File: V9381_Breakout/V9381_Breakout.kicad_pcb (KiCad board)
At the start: 2 copper layers, 38.1 x 27.9 mm, 2 parts, among them J1 Conn_01x10

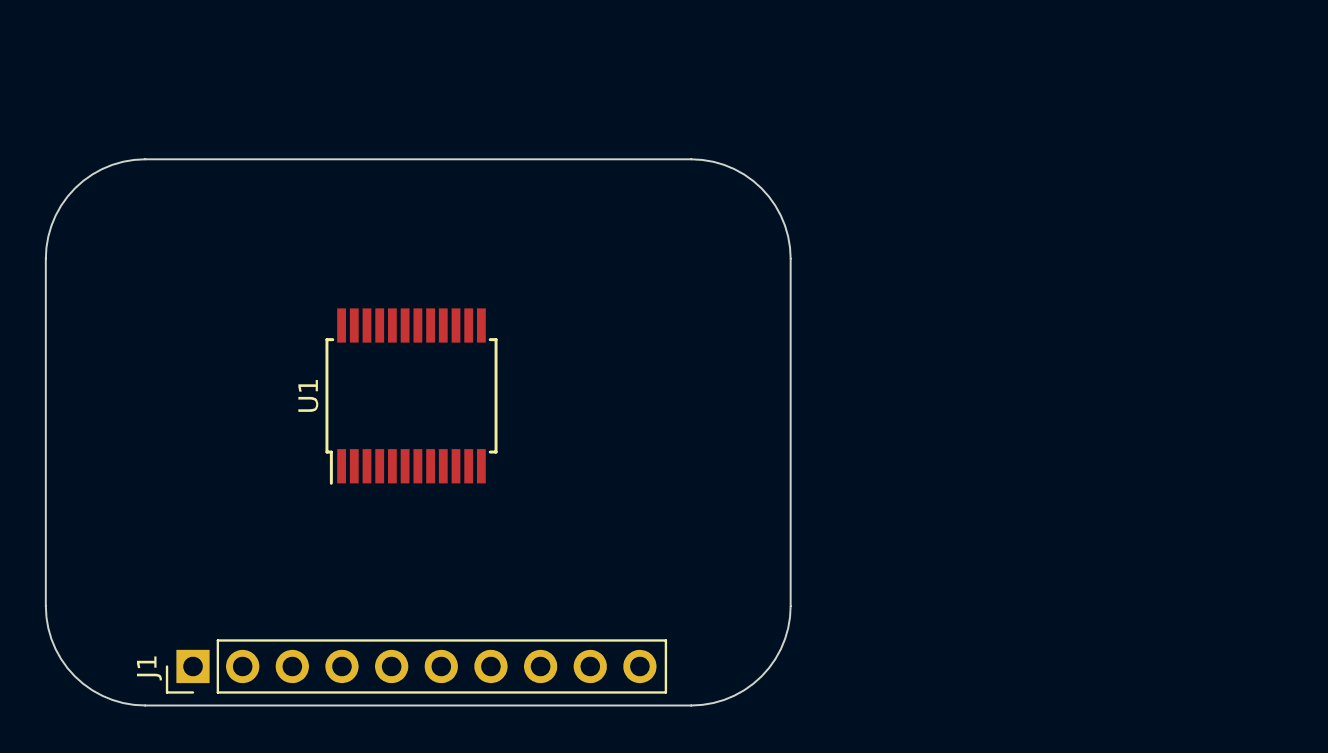
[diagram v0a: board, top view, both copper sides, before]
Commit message: Start the wiring up and PCB outline
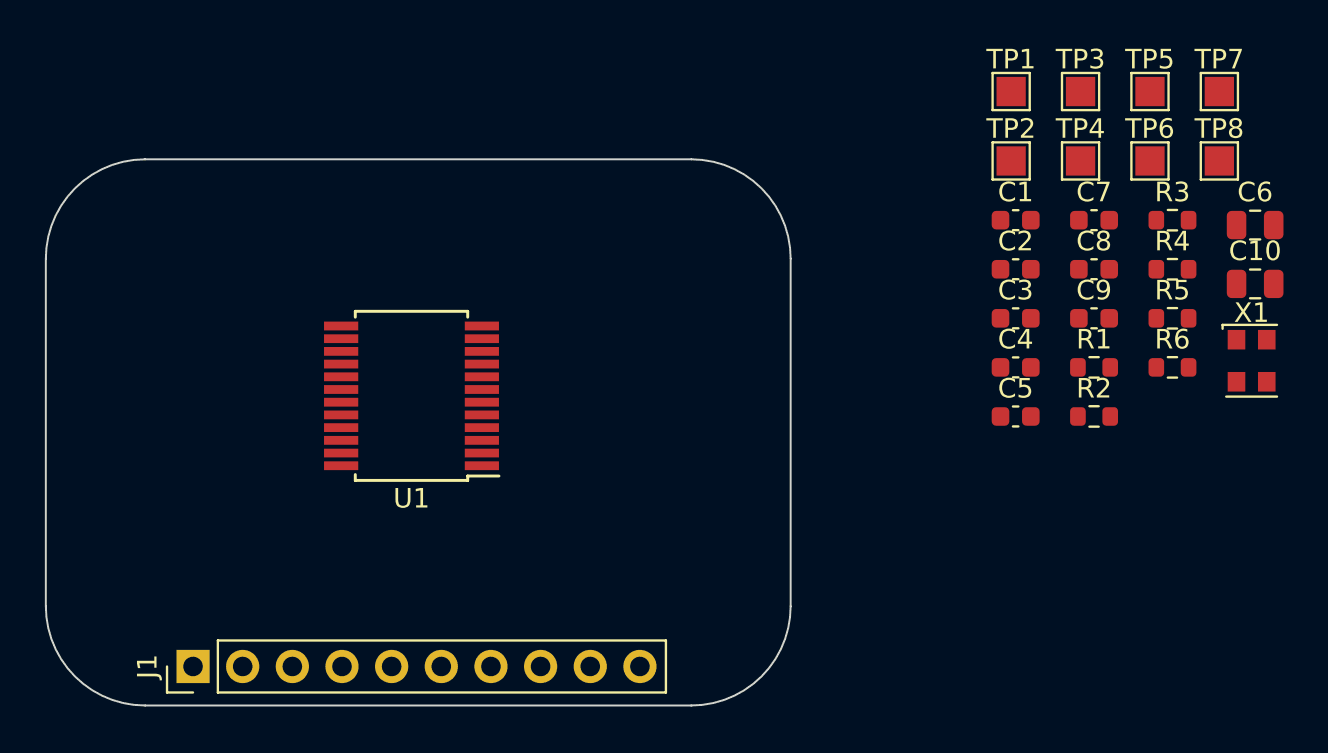
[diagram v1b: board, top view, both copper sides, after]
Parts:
- added C1: 33n, Capacitor_SMD:C_0603_1608Metric, F.Cu at (176.7, 83.5)
- added C10: 4.7u, Capacitor_SMD:C_0805_2012Metric, F.Cu at (189.0, 86.7)
- added C2: 33n, Capacitor_SMD:C_0603_1608Metric, F.Cu at (176.7, 86.0)
- added C3: 100p, Capacitor_SMD:C_0603_1608Metric, F.Cu at (176.7, 88.5)
- added C4: 33n, Capacitor_SMD:C_0603_1608Metric, F.Cu at (176.7, 91.0)
- added C5: 33n, Capacitor_SMD:C_0603_1608Metric, F.Cu at (176.7, 93.5)
- added C6: 4.7u, Capacitor_SMD:C_0805_2012Metric, F.Cu at (189.0, 83.7)
- added C7: 100n, Capacitor_SMD:C_0603_1608Metric, F.Cu at (180.7, 83.5)
- added C8: 100n, Capacitor_SMD:C_0603_1608Metric, F.Cu at (180.7, 86.0)
- added C9: 100n, Capacitor_SMD:C_0603_1608Metric, F.Cu at (180.7, 88.5)
- added R1: 2R2, Resistor_SMD:R_0603_1608Metric, F.Cu at (180.7, 91.0)
- added R2: 2R2, Resistor_SMD:R_0603_1608Metric, F.Cu at (180.7, 93.5)
- added R3: 1k, Resistor_SMD:R_0603_1608Metric, F.Cu at (184.7, 83.5)
- added R4: 1k, Resistor_SMD:R_0603_1608Metric, F.Cu at (184.7, 86.0)
- added R5: 1k, Resistor_SMD:R_0603_1608Metric, F.Cu at (184.7, 88.5)
- added R6: 1k, Resistor_SMD:R_0603_1608Metric, F.Cu at (184.7, 91.0)
- added TP1: TestPoint, TestPoint:TestPoint_Pad_1.5x1.5mm, F.Cu at (176.5, 76.9)
- added TP2: TestPoint, TestPoint:TestPoint_Pad_1.5x1.5mm, F.Cu at (176.5, 80.4)
- added TP3: TestPoint, TestPoint:TestPoint_Pad_1.5x1.5mm, F.Cu at (180.0, 76.9)
- added TP4: TestPoint, TestPoint:TestPoint_Pad_1.5x1.5mm, F.Cu at (180.0, 80.4)
- added TP5: TestPoint, TestPoint:TestPoint_Pad_1.5x1.5mm, F.Cu at (183.6, 76.9)
- added TP6: TestPoint, TestPoint:TestPoint_Pad_1.5x1.5mm, F.Cu at (183.6, 80.4)
- added TP7: TestPoint, TestPoint:TestPoint_Pad_1.5x1.5mm, F.Cu at (187.1, 76.9)
- added TP8: TestPoint, TestPoint:TestPoint_Pad_1.5x1.5mm, F.Cu at (187.1, 80.4)
- added X1: XO32, Oscillator:Oscillator_SMD_EuroQuartz_XO32-4Pin_3.2x2.5mm, F.Cu at (188.8, 90.7)
- turned U1 to 180 degrees
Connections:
- J1 pad 7: UN_IN -> GND
- U1 pad 1: unconnected-(U1-CTI-Pad1) -> Net-(U1-CTI)
- U1 pad 10: unconnected-(U1-VSS-Pad10) -> GND
- U1 pad 11: unconnected-(U1-DVCC-Pad11) -> Net-(U1-DVCC)
- U1 pad 12: unconnected-(U1-VREF-Pad12) -> Net-(U1-VREF)
- U1 pad 15: unconnected-(U1-P6-Pad15) -> P6
- U1 pad 16: unconnected-(U1-P5-Pad16) -> P5
- U1 pad 17: unconnected-(U1-P3-Pad17) -> P3
- U1 pad 18: unconnected-(U1-P2-Pad18) -> P2
- U1 pad 19: unconnected-(U1-RX/MOSI-Pad19) -> RX/MOSI
- U1 pad 20: unconnected-(U1-TX/MISO-Pad20) -> TX/MISO
- U1 pad 21: unconnected-(U1-A1/SPCSN-Pad21) -> CS
- U1 pad 22: unconnected-(U1-A0/SPCK-Pad22) -> SCK
- U1 pad 23: unconnected-(U1-P1-Pad23) -> P1
- U1 pad 24: unconnected-(U1-P0-Pad24) -> P0
- U1 pad 3: unconnected-(U1-UP-Pad3) -> UP
- U1 pad 4: unconnected-(U1-UN-Pad4) -> UN
- U1 pad 5: unconnected-(U1-IBN-Pad5) -> IBN
- U1 pad 6: unconnected-(U1-IBP-Pad6) -> IBP
- U1 pad 7: unconnected-(U1-IAN-Pad7) -> IAN
- U1 pad 8: unconnected-(U1-IAP-Pad8) -> IAP
- U1 pad 9: unconnected-(U1-VDD-Pad9) -> VIN

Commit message: Finish routing
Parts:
- added TP10: TestPoint, TestPoint:TestPoint_Pad_1.5x1.5mm, B.Cu at (130.3, 87.6)
- added TP9: TestPoint, TestPoint:TestPoint_Pad_1.5x1.5mm, B.Cu at (130.3, 90.4)
- TP1, TP2, TP3, TP4, TP5, TP6, TP7, TP8: moved to B.Cu
- moved TP7 60.0 mm to (130.3, 96.0), turned to -90 degrees
- moved TP5 58.7 mm to (130.3, 101.6), turned to -90 degrees
- moved TP8 58.2 mm to (130.3, 93.2), turned to -90 degrees
- moved TP6 56.3 mm to (130.3, 98.8), turned to -90 degrees
- moved TP3 52.4 mm to (133.9, 101.6), turned to -90 degrees
- moved TP4 49.7 mm to (133.9, 98.8), turned to -90 degrees
- moved C6 44.0 mm to (145.0, 85.9)
- moved X1 42.9 mm to (146.8, 99.6), turned to 180 degrees
- moved C10 39.6 mm to (149.4, 87.4), turned to 90 degrees
- moved R5 36.1 mm to (150.9, 101.1)
- moved C7 35.7 mm to (145.0, 83.3)
- moved R3 32.6 mm to (154.4, 95.2), turned to 180 degrees
- moved R6 32.2 mm to (154.2, 101.1), turned to 180 degrees
- moved C8 31.7 mm to (149.4, 90.9)
- moved R4 30.7 mm to (154.4, 90.7), turned to 180 degrees
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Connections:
- U1 pad 13: unconnected-(U1-32KIN-Pad13) -> 32KIN
- U1 pad 14: unconnected-(U1-RSTN-Pad14) -> ~{RST}
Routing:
- net VIN: track 0.00 -> 34.1 mm
- net IBP: track 0.00 -> 24.1 mm, vias 0 -> 1
- net IAP_IN: track 0.00 -> 21.8 mm
- net GND: track 0.00 -> 20.6 mm, vias 0 -> 7
- net IBN: track 0.00 -> 20.3 mm, vias 0 -> 1
- net TX/MISO: track 0.00 -> 16.3 mm, vias 0 -> 1
- net CS: track 0.00 -> 16.3 mm
- net RX/MOSI: track 0.00 -> 16.1 mm
- net P2: track 0.00 -> 15.0 mm, vias 0 -> 1
- net IAN_IN: track 0.00 -> 14.1 mm
- net IAN: track 0.00 -> 13.4 mm
- net SCK: track 0.00 -> 13.2 mm
- net P3: track 0.00 -> 12.7 mm, vias 0 -> 1
- net UN: track 0.00 -> 11.5 mm
- net P5: track 0.00 -> 11.1 mm, vias 0 -> 1
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- added copper zone on B.Cu, net GND
- added copper zone on F.Cu, net GND
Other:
- outline, holes or cut-outs redrawn
- board text added: "32KIN"
- board text added: "GND"
- board text added: "IAN"
- board text added: "IAP"
- board text added: "IBN"
- board text added: "IBP"
- board text added: "P0"
- board text added: "P1"
- board text added: "P2"
- board text added: "P3"
- board text added: "P5"
- board text added: "P6"
- board text added: "RX/MO"
- board text added: "SCK"
- board text added: "TX/MI"
- board text added: "UN"
- board text added: "UP"
- board text added: "VIN"
- board text added: "~{CS}"
- board text added: "~{RST}"

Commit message: Finish routing and create fab outputs
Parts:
- added SYM1: Logo_Open_Hardware_Small, Symbol:OSHW-Logo2_9.8x8mm_SilkScreen, B.Cu at (146.3, 95.0)
- U1: value ~ -> V9381
- moved C7 0.57 mm to (145.3, 83.8)
- moved X1 0.06 mm to (146.8, 99.6)
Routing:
- net GND: track 20.6 -> 23.7 mm, vias 7 -> 22
- net IAN: track 13.4 -> 10.8 mm
- net VIN: track 34.1 -> 31.6 mm, vias 0 -> 1
- net Net-(U1-VREF): track 7.04 -> 6.49 mm
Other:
- outline, holes or cut-outs redrawn
- board text added: "A0/SCK"
- board text added: "A1/~{CS}"
- board text added: "MAX Vrms = 140mV V9381 Breakout"
- board text added: "by Tisham Dhar https://whatnick.com v0.1 08/03/2025"
- board text removed: "SCK"
- board text removed: "~{CS}"
